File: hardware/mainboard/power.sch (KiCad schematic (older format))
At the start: 13 parts, among them U1 LM4040DBZ-10, U2 LM1117-3.3

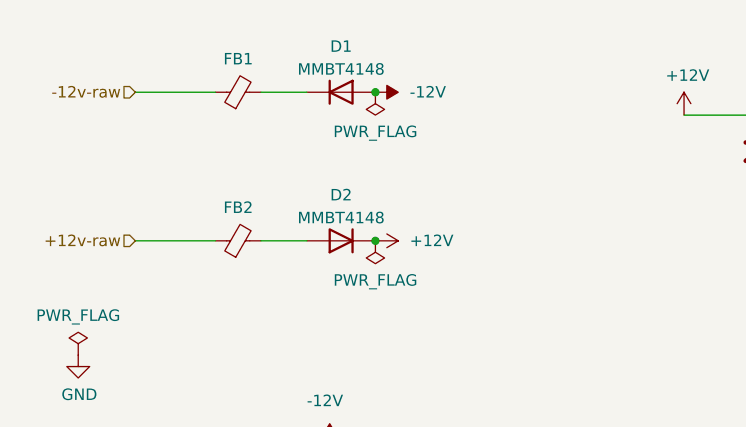
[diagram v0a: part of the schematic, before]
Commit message: hardware: assign new MPNs for mainboard BOM
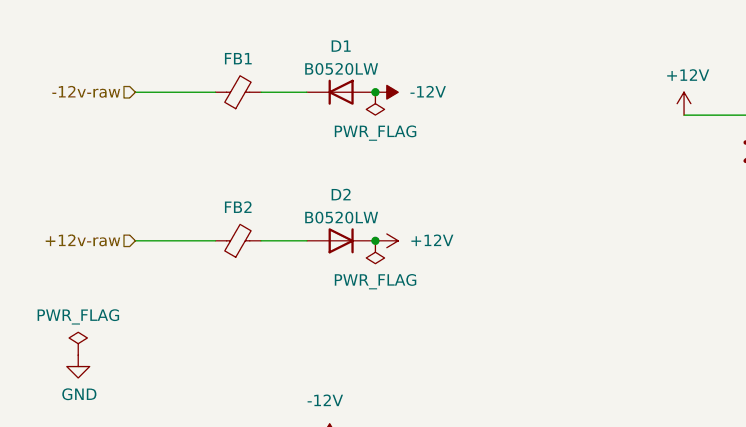
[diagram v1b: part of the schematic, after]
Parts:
- C2, C3: finalized yes -> yes & alt
- C48: finalized yes -> yes & alt; mpn CL21A226MAQNNN -> C2012X5R1V226M125AC; mpn alt GRM21BR61E226ME44L -> CL21A226MAQNNN
- D1, D2: value MMBT4148 -> B0520LW; Reqs (none) -> Schottky, 1A; mpn MF-DIO-SOD123-1N4148 -> B0520LWQ-7-F; mpn alt 1N4148W-7-F -> (none)
- FB1, FB2, FB3: value Ferrite_Bead_Small -> Ferrite Bead; Reqs (none) -> >500mA DC current; mpn 710-742792664 -> 742792651; mpn specs 300mA, 600 mOhms DC, 1 kOhms AC -> (none)
- R1: mpn alt (none) -> ERA-3AED222V
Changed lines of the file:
@@
 P 2250 1100
 F 0 "D1" H 2250 1300 50  0000 C CNN
-F 1 "MMBT4148" H 2250 1200 50  0000 C CNN
+F 1 "B0520LW" H 2250 1200 50  0000 C CNN
 F 2 "Diode_SMD:D_SOD-123" H 2250 1100 50  0001 C CNN
 F 3 "~" H 2250 1100 50  0001 C CNN
 F 4 "yes" H 2250 1100 50  0001 C CNN "finalized"
-F 5 "MF-DIO-SOD123-1N4148" H 2250 1100 50  0001 C CNN "mpn"
-F 6 "1N4148W-7-F" H 2250 1100 50  0001 C CNN "mpn alt"
+F 5 "B0520LWQ-7-F" H 2250 1100 50  0001 C CNN "mpn"
+F 6 "" H 2250 1100 50  0001 C CNN "mpn alt"
+F 7 "Schottky, 1A" H 2250 1100 50  0001 C CNN "Reqs"
 	1    2250 1100
 	1    0    0    -1
@@
 P 2250 1750
 F 0 "D2" H 2250 1550 50  0000 C CNN
-F 1 "MMBT4148" H 2250 1650 50  0000 C CNN
+F 1 "B0520LW" H 2250 1650 50  0000 C CNN
 F 2 "Diode_SMD:D_SOD-123" H 2250 1750 50  0001 C CNN
 F 3 "~" H 2250 1750 50  0001 C CNN
 F 4 "yes" H 2250 1750 50  0001 C CNN "finalized"
-F 5 "MF-DIO-SOD123-1N4148" H 2250 1750 50  0001 C CNN "mpn"
-F 6 "1N4148W-7-F" H 2250 1750 50  0001 C CNN "mpn alt"
+F 5 "B0520LWQ-7-F" H 2250 1750 50  0001 C CNN "mpn"
+F 6 "" H 2250 1750 50  0001 C CNN "mpn alt"
+F 7 "Schottky, 1A" H 2250 1750 50  0001 C CNN "Reqs"
 	1    2250 1750
 	-1   0    0    1
@@
 F 4 "ESR 0.3-22 Ohms, 16v+" H 5200 1350 50  0001 C CNN "Reqs"
 F 5 "EEE-FK1V470P" H 5200 1350 50  0001 C CNN "mpn"
-F 6 "yes" H 5200 1350 50  0001 C CNN "finalized"
+F 6 "yes & alt" H 5200 1350 50  0001 C CNN "finalized"
 F 7 "20%, 35v, 0.36 Ohms" H 5200 1350 50  0001 C CNN "mpn specs"
 F 8 "EEE-FK1H470XP" H 5200 1350 50  0001 C CNN "mpn alt"
@@
 P 5950 1100
 F 0 "FB3" H 5850 1100 50  0000 R CNN
-F 1 "Ferrite_Bead_Small" H 5850 1145 50  0001 R CNN
+F 1 "Ferrite Bead" H 5850 1145 50  0001 R CNN
 F 2 "Inductor_SMD:L_0603_1608Metric_Pad1.05x0.95mm_HandSolder" V 5880 1100 50  0001 C CNN
 F 3 "~" H 5950 1100 50  0001 C CNN
-F 4 "710-742792664" H 5950 1100 50  0001 C CNN "mpn"
+F 4 "742792651" H 5950 1100 50  0001 C CNN "mpn"
 F 5 "yes" H 5950 1100 50  0001 C CNN "finalized"
-F 6 "300mA, 600 mOhms DC, 1 kOhms AC" H 5950 1100 50  0001 C CNN "mpn specs"
+F 6 "" H 5950 1100 50  0001 C CNN "mpn specs"
+F 7 ">500mA DC current" H 5950 1100 50  0001 C CNN "Reqs"
 	1    5950 1100
 	-1   0    0    1
@@
 F 3 "~" H 4100 1350 50  0001 C CNN
 F 4 "EEE-FK1V470P" H 4100 1350 50  0001 C CNN "mpn"
-F 5 "yes" H 4100 1350 50  0001 C CNN "finalized"
+F 5 "yes & alt" H 4100 1350 50  0001 C CNN "finalized"
 F 6 "ESR 0.3-22 Ohms, 16v+" H 4100 1350 50  0001 C CNN "Reqs"
 F 7 "20%, 35v, 0.36 Ohms" H 4100 1350 50  0001 C CNN "mpn specs"
@@
 P 1800 1750
 F 0 "FB2" V 1945 1750 50  0000 C CNN
-F 1 "Ferrite_Bead_Small" V 1946 1750 50  0001 C CNN
+F 1 "Ferrite Bead" V 1946 1750 50  0001 C CNN
 F 2 "Inductor_SMD:L_0603_1608Metric_Pad1.05x0.95mm_HandSolder" V 1730 1750 50  0001 C CNN
 F 3 "~" H 1800 1750 50  0001 C CNN
-F 4 "710-742792664" H 1800 1750 50  0001 C CNN "mpn"
+F 4 "742792651" H 1800 1750 50  0001 C CNN "mpn"
 F 5 "yes" H 1800 1750 50  0001 C CNN "finalized"
-F 6 "300mA, 600 mOhms DC, 1 kOhms AC" H 1800 1750 50  0001 C CNN "mpn specs"
+F 6 "" H 1800 1750 50  0001 C CNN "mpn specs"
+F 7 ">500mA DC current" H 1800 1750 50  0001 C CNN "Reqs"
 	1    1800 1750
 	0    -1   -1   0
@@
 F 6 "1%, 60mW, vref current control" H 2200 2800 50  0001 C CNN "Reqs"
 F 7 "125mW,  1%" H 2200 2800 50  0001 C CNN "mpn specs"
+F 8 "ERA-3AED222V" H 2200 2800 50  0001 C CNN "mpn alt"
 	1    2200 2800
 	1    0    0    -1
@@
 P 1800 1100
 F 0 "FB1" V 1945 1100 50  0000 C CNN
-F 1 "Ferrite_Bead_Small" V 1946 1100 50  0001 C CNN
+F 1 "Ferrite Bead" V 1946 1100 50  0001 C CNN
 F 2 "Inductor_SMD:L_0603_1608Metric_Pad1.05x0.95mm_HandSolder" V 1730 1100 50  0001 C CNN
 F 3 "~" H 1800 1100 50  0001 C CNN
-F 4 "710-742792664" H 1800 1100 50  0001 C CNN "mpn"
+F 4 "742792651" H 1800 1100 50  0001 C CNN "mpn"
 F 5 "yes" H 1800 1100 50  0001 C CNN "finalized"
-F 6 "300mA, 600 mOhms DC, 1 kOhms AC" H 1800 1100 50  0001 C CNN "mpn specs"
+F 6 "" H 1800 1100 50  0001 C CNN "mpn specs"
+F 7 ">500mA DC current" H 1800 1100 50  0001 C CNN "Reqs"
 	1    1800 1100
 	0    -1   -1   0
@@
 F 2 "Capacitor_SMD:C_0805_2012Metric_Pad1.15x1.40mm_HandSolder" H 4438 2800 50  0001 C CNN
 F 3 "~" H 4400 2950 50  0001 C CNN
-F 4 "CL21A226MAQNNN" H 4400 2950 50  0001 C CNN "mpn"
-F 5 "yes" H 4400 2950 50  0001 C CNN "finalized"
+F 4 "C2012X5R1V226M125AC" H 4400 2950 50  0001 C CNN "mpn"
+F 5 "yes & alt" H 4400 2950 50  0001 C CNN "finalized"
 F 6 "22uF 20% 25v" H 4400 2950 50  0001 C CNN "mpn specs"
 F 7 "power bypass, 25v" H 4400 2950 50  0001 C CNN "Reqs"
-F 8 "GRM21BR61E226ME44L" H 4400 2950 50  0001 C CNN "mpn alt"
+F 8 "CL21A226MAQNNN" H 4400 2950 50  0001 C CNN "mpn alt"
 	1    4400 2950
 	1    0    0    -1
